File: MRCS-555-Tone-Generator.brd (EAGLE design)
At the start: 50 x 50 mm, 19 parts, among them CON1 5V input, CON2 5 V input, CON3 output 3.5mm, CON4 Output 0.100, IC1 NE555

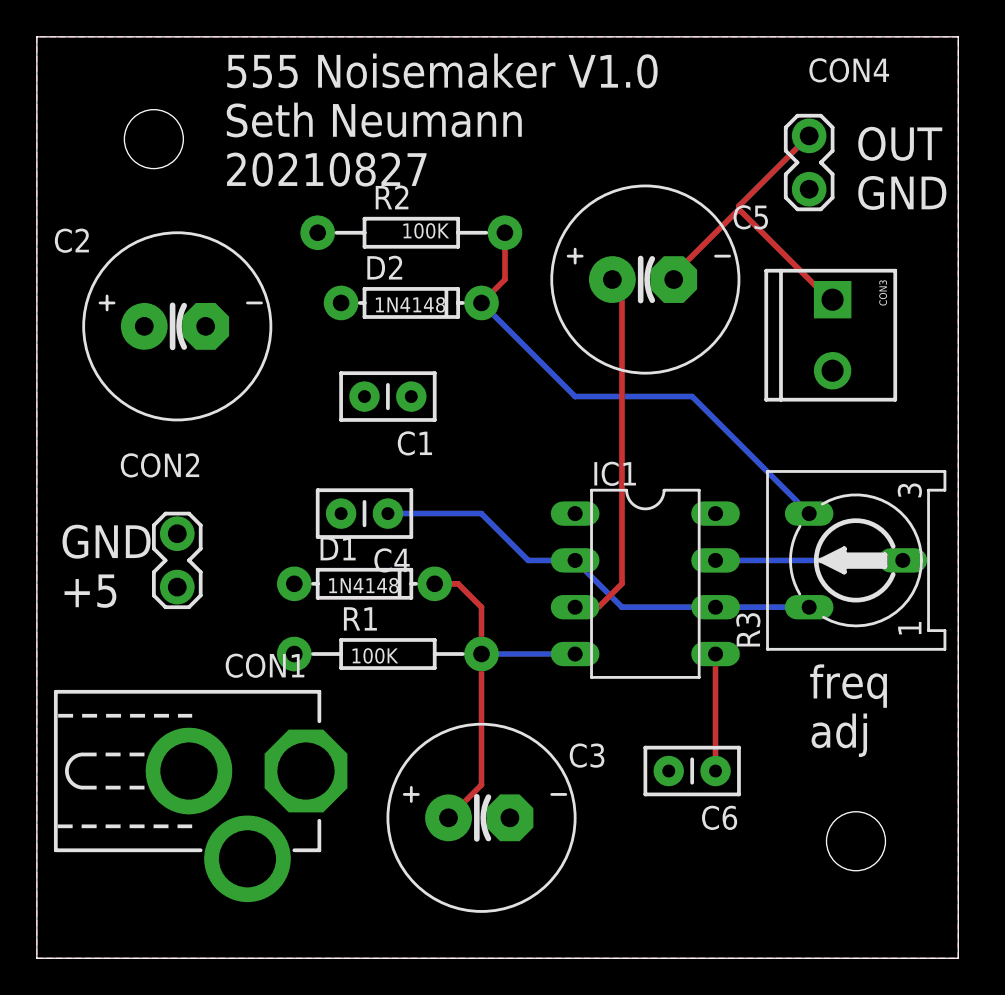
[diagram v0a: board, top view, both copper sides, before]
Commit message: Updates after first article tested good
clean up of some nomenclature
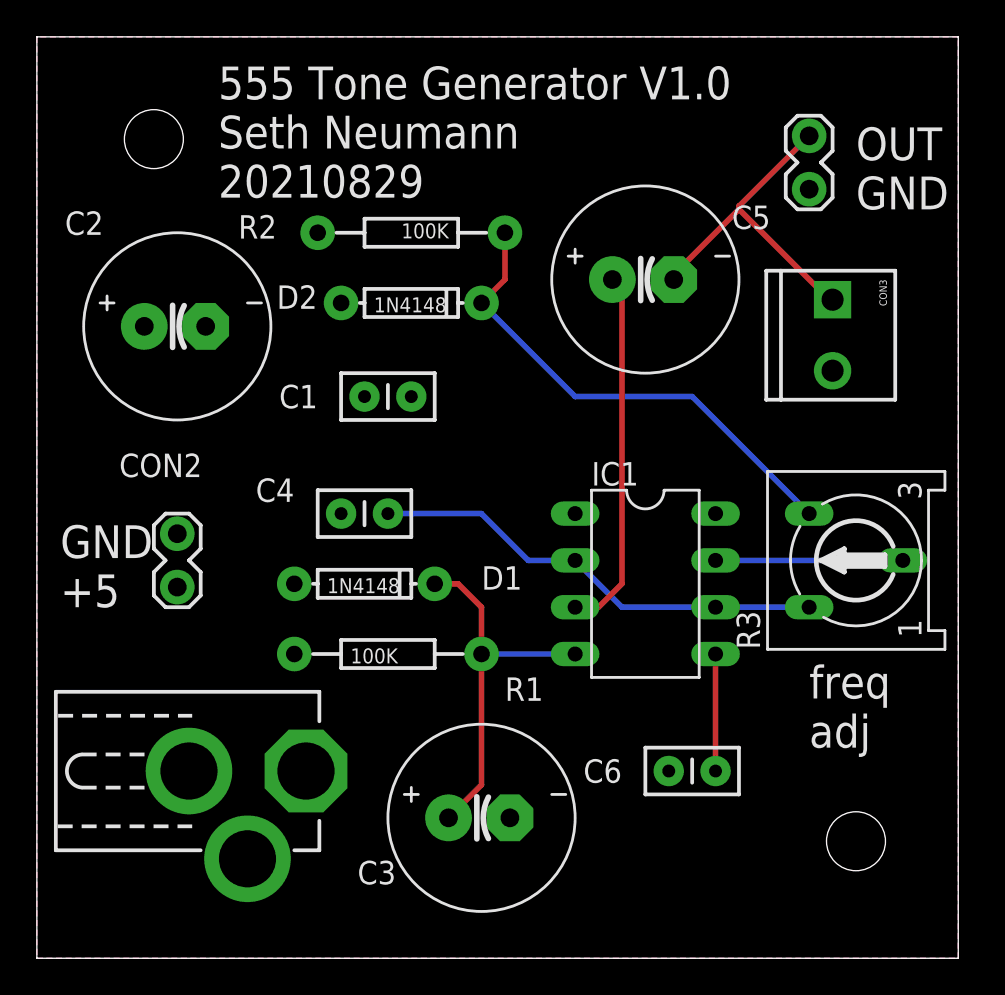
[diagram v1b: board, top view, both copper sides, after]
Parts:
- C1: value 0.01 uF 103 -> .01uF
- C4: value 0.01 103 -> 0.01uF
- C6: value 0.01 uF 103 -> 0.01uF
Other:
- board text added: "555 Tone Generator V1.0 Seth Neumann 20210829"
- board text removed: "555 Noisemaker V1.0 Seth Neumann 20210827"
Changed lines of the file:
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@@
 <setting verticaltext="up"/>
 </settings>
-<grid distance="25" unitdist="mil" unit="mil" style="dots" multiple="2" display="yes" altdistance="12.5" altunitdist="mil" altunit="mil"/>
+<grid distance="50" unitdist="mil" unit="mil" style="dots" multiple="2" display="yes" altdistance="12.5" altunitdist="mil" altunit="mil"/>
 <layers>
 <layer number="1" name="Top" color="4" fill="1" visible="yes" active="yes"/>
@@
 <hole x="6.35" y="44.45" drill="3.2"/>
 <hole x="44.45" y="6.35" drill="3.2"/>
-<text x="10.16" y="41.91" size="1.778" layer="21" font="vector" ratio="10">555 Noisemaker V1.0
+<text x="9.8425" y="41.275" size="1.778" layer="21" font="vector" ratio="10">555 Tone Generator V1.0
 Seth Neumann
-20210827</text>
+20210829</text>
 <text x="41.91" y="11.43" size="1.778" layer="21" font="vector" ratio="10">freq
 adj</text>
@@
 <element name="CON2" library="SPCoast" package="1X02_LOCK" value="5 V input" x="7.62" y="20.32" smashed="yes" rot="R90">
 <attribute name="NAME" x="8.9662" y="27.3812" size="1.27" layer="25" ratio="10" rot="R180"/>
-<attribute name="VALUE" x="12.065" y="19.05" size="1.27" layer="27" rot="R90"/>
 </element>
 <element name="CON3" library="SPCoast" package="SCREWTERMINAL-3.5MM-2_LOCK" value="output 3.5mm" x="43.18" y="35.56" rot="R270"/>
 <element name="D1" library="SPCoast" package="DIODE-1N4148" value="1N4148" x="17.78" y="20.32" smashed="yes" rot="R180">
-<attribute name="NAME" x="15.24" y="21.59" size="1.27" layer="25"/>
+<attribute name="NAME" x="24.13" y="20.0025" size="1.27" layer="25"/>
 <attribute name="VALUE" x="15.748" y="19.812" size="0.8128" layer="21"/>
 </element>
 <element name="D2" library="SPCoast" package="DIODE-1N4148" value="1N4148" x="20.32" y="35.56" smashed="yes" rot="R180">
-<attribute name="NAME" x="17.78" y="36.83" size="1.27" layer="25"/>
+<attribute name="NAME" x="13.0175" y="35.2425" size="1.27" layer="25"/>
 <attribute name="VALUE" x="18.288" y="35.052" size="0.8128" layer="21"/>
 </element>
@@
 </element>
 <element name="R2" library="SPCoast" package="AXIAL-0.4-RES" value="100K" x="20.32" y="39.37" smashed="yes" rot="R180">
-<attribute name="NAME" x="20.32" y="41.91" size="1.27" layer="25" rot="R180"/>
+<attribute name="NAME" x="13.0175" y="40.3225" size="1.27" layer="25" rot="R180"/>
 <attribute name="VALUE" x="22.352" y="39.878" size="0.8128" layer="21" ratio="15" rot="R180"/>
 </element>
 <element name="R1" library="SPCoast" package="AXIAL-0.4-RES" value="100K" x="19.05" y="16.51" smashed="yes">
-<attribute name="NAME" x="16.51" y="17.78" size="1.27" layer="25"/>
+<attribute name="NAME" x="25.4" y="13.97" size="1.27" layer="25"/>
 <attribute name="VALUE" x="17.018" y="16.002" size="0.8128" layer="21" ratio="15"/>
 </element>
 <element name="C2" library="SPCoast" package="E3.5-10" value="100 uF" x="7.62" y="34.29" smashed="yes">
-<attribute name="NAME" x="0.889" y="38.3032" size="1.27" layer="25" ratio="10"/>
+<attribute name="NAME" x="1.524" y="39.2557" size="1.27" layer="25" ratio="10"/>
 <attribute name="VALUE" x="4.4958" y="31.0642" size="1.27" layer="27" ratio="10"/>
 </element>
-<element name="C4" library="SPCoast" package="C-PTH-0.100" value="0.01 103" x="17.78" y="24.13" smashed="yes" rot="R180">
-<attribute name="NAME" x="20.32" y="22.225" size="1.27" layer="25" rot="R180"/>
-<attribute name="VALUE" x="20.32" y="26.67" size="0.6096" layer="27" rot="R180"/>
+<element name="C4" library="SPCoast" package="C-PTH-0.100" value="0.01uF" x="17.78" y="24.13" smashed="yes" rot="R180">
+<attribute name="NAME" x="13.97" y="26.035" size="1.27" layer="25" rot="R180"/>
+<attribute name="VALUE" x="26.67" y="25.4" size="1.27" layer="27" rot="R180"/>
 </element>
 <element name="R3" library="MRCS" package="RS3" value="100K" x="44.45" y="21.59" rot="R90"/>
-<element name="CON1" library="SPCoast" package="DCJ0202" value="5V input" x="11.43" y="10.16" rot="R270"/>
-<element name="CON4" library="SPCoast" package="1X02_LOCK" value="Output 0.100" x="41.91" y="44.45" smashed="yes" rot="R270">
-<attribute name="NAME" x="41.8338" y="47.5488" size="1.27" layer="25" ratio="10"/>
-</element>
-<element name="C1" library="SPCoast" package="C-PTH-0.100" value="0.01 uF 103" x="19.05" y="30.48" smashed="yes" rot="R180">
-<attribute name="NAME" x="21.59" y="28.575" size="1.27" layer="25" rot="R180"/>
-<attribute name="VALUE" x="21.59" y="33.02" size="0.6096" layer="27" rot="R180"/>
-</element>
-<element name="C6" library="SPCoast" package="C-PTH-0.100" value="0.01 uF 103" x="35.56" y="10.16" smashed="yes" rot="R180">
-<attribute name="NAME" x="38.1" y="8.255" size="1.27" layer="25" rot="R180"/>
-<attribute name="VALUE" x="38.1" y="12.7" size="0.6096" layer="27" rot="R180"/>
+<element name="CON1" library="SPCoast" package="DCJ0202" value="5V input" x="11.43" y="10.16" smashed="yes" rot="R270">
+<attribute name="VALUE" x="1.27" y="15.24" size="1.27" layer="27"/>
+</element>
+<element name="CON4" library="SPCoast" package="1X02_LOCK" value="Output 0.100" x="41.91" y="44.45" smashed="yes" rot="R270"/>
+<element name="C1" library="SPCoast" package="C-PTH-0.100" value=".01uF" x="19.05" y="30.48" smashed="yes" rot="R180">
+<attribute name="NAME" x="15.24" y="31.115" size="1.27" layer="25" rot="R180"/>
+<attribute name="VALUE" x="26.67" y="31.75" size="1.27" layer="27" rot="R180"/>
+</element>
+<element name="C6" library="SPCoast" package="C-PTH-0.100" value="0.01uF " x="35.56" y="10.16" smashed="yes" rot="R180">
+<attribute name="NAME" x="31.75" y="10.795" size="1.27" layer="25" rot="R180"/>
+<attribute name="VALUE" x="39.37" y="13.97" size="1.27" layer="27" rot="R180"/>
 </element>
 <element name="C5" library="SPCoast" package="E3.5-10" value="100 uF" x="33.02" y="36.83"/>
-<element name="C3" library="SPCoast" package="E3.5-10" value="10 uF" x="24.13" y="7.62"/>
+<element name="C3" library="SPCoast" package="E3.5-10" value="10 uF" x="24.13" y="7.62" smashed="yes">
+<attribute name="NAME" x="17.399" y="4.0132" size="1.27" layer="25" ratio="10"/>
+<attribute name="VALUE" x="21.0058" y="4.3942" size="1.27" layer="27" ratio="10"/>
+</element>
 <element name="U$1" library="MRCSLogoTop" package="MRCSLOGOTOP" value="" x="31.75" y="1.27"/>
 <element name="U$2" library="MRCSLogoBtm" package="MRCSLOGOBTM" value="" x="31.75" y="1.27"/>

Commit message: Minor updates after building 1st articles
Changed C3 from electrolytic to 0.1 for Tant or Monolithic
Minor clean up of labels on board
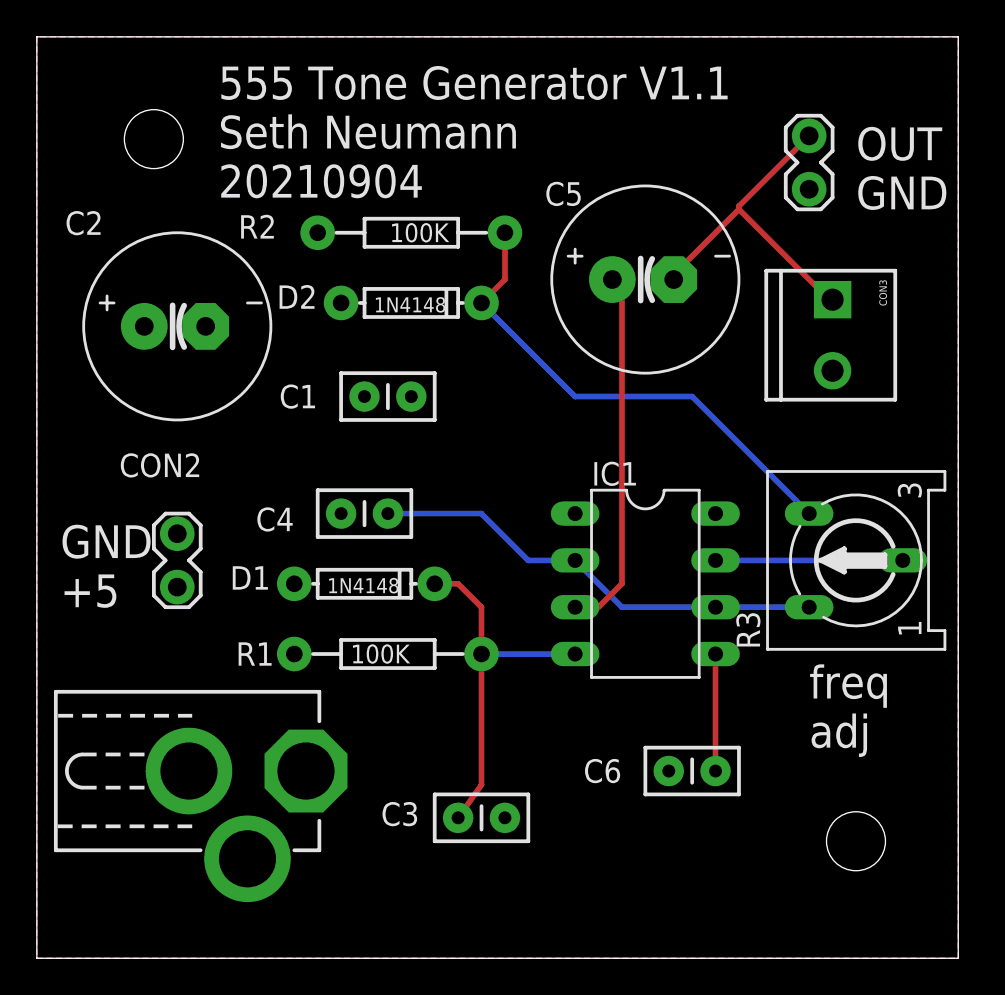
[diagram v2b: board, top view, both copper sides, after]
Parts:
- C1: value .01uF -> 0.01uF
- C3: device SPCoast:E3.5-10 -> SPCoast:C-PTH-0.100
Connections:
- net GND: now also C3.2; no longer C3.-
- net N$6: now also C3.1; no longer C3.+
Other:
- board text added: "555 Tone Generator V1.1 Seth Neumann 20210904"
- board text removed: "555 Tone Generator V1.0 Seth Neumann 20210829"
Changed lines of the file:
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@@
 <hole x="6.35" y="44.45" drill="3.2"/>
 <hole x="44.45" y="6.35" drill="3.2"/>
-<text x="9.8425" y="41.275" size="1.778" layer="21" font="vector" ratio="10">555 Tone Generator V1.0
+<text x="9.8425" y="41.275" size="1.778" layer="21" font="vector" ratio="10">555 Tone Generator V1.1
 Seth Neumann
-20210829</text>
+20210904</text>
 <text x="41.91" y="11.43" size="1.778" layer="21" font="vector" ratio="10">freq
 adj</text>
@@
 <element name="CON3" library="SPCoast" package="SCREWTERMINAL-3.5MM-2_LOCK" value="output 3.5mm" x="43.18" y="35.56" rot="R270"/>
 <element name="D1" library="SPCoast" package="DIODE-1N4148" value="1N4148" x="17.78" y="20.32" smashed="yes" rot="R180">
-<attribute name="NAME" x="24.13" y="20.0025" size="1.27" layer="25"/>
+<attribute name="NAME" x="10.4775" y="20.0025" size="1.27" layer="25"/>
 <attribute name="VALUE" x="15.748" y="19.812" size="0.8128" layer="21"/>
 </element>
@@
 <element name="R2" library="SPCoast" package="AXIAL-0.4-RES" value="100K" x="20.32" y="39.37" smashed="yes" rot="R180">
 <attribute name="NAME" x="13.0175" y="40.3225" size="1.27" layer="25" rot="R180"/>
-<attribute name="VALUE" x="22.352" y="39.878" size="0.8128" layer="21" ratio="15" rot="R180"/>
+<attribute name="VALUE" x="22.352" y="39.878" size="1.016" layer="21" ratio="15" rot="R180"/>
 </element>
 <element name="R1" library="SPCoast" package="AXIAL-0.4-RES" value="100K" x="19.05" y="16.51" smashed="yes">
-<attribute name="NAME" x="25.4" y="13.97" size="1.27" layer="25"/>
-<attribute name="VALUE" x="17.018" y="16.002" size="0.8128" layer="21" ratio="15"/>
+<attribute name="NAME" x="10.795" y="15.875" size="1.27" layer="25"/>
+<attribute name="VALUE" x="17.018" y="16.002" size="1.016" layer="21" ratio="15"/>
 </element>
 <element name="C2" library="SPCoast" package="E3.5-10" value="100 uF" x="7.62" y="34.29" smashed="yes">
@@
 </element>
 <element name="C4" library="SPCoast" package="C-PTH-0.100" value="0.01uF" x="17.78" y="24.13" smashed="yes" rot="R180">
-<attribute name="NAME" x="13.97" y="26.035" size="1.27" layer="25" rot="R180"/>
+<attribute name="NAME" x="13.97" y="24.4475" size="1.27" layer="25" rot="R180"/>
 <attribute name="VALUE" x="26.67" y="25.4" size="1.27" layer="27" rot="R180"/>
 </element>
@@
 </element>
 <element name="CON4" library="SPCoast" package="1X02_LOCK" value="Output 0.100" x="41.91" y="44.45" smashed="yes" rot="R270"/>
-<element name="C1" library="SPCoast" package="C-PTH-0.100" value=".01uF" x="19.05" y="30.48" smashed="yes" rot="R180">
+<element name="C1" library="SPCoast" package="C-PTH-0.100" value="0.01uF" x="19.05" y="30.48" smashed="yes" rot="R180">
 <attribute name="NAME" x="15.24" y="31.115" size="1.27" layer="25" rot="R180"/>
-<attribute name="VALUE" x="26.67" y="31.75" size="1.27" layer="27" rot="R180"/>
+<attribute name="VALUE" x="27.94" y="31.75" size="1.27" layer="27" rot="R180"/>
 </element>
 <element name="C6" library="SPCoast" package="C-PTH-0.100" value="0.01uF " x="35.56" y="10.16" smashed="yes" rot="R180">
@@
 <attribute name="VALUE" x="39.37" y="13.97" size="1.27" layer="27" rot="R180"/>
 </element>
-<element name="C5" library="SPCoast" package="E3.5-10" value="100 uF" x="33.02" y="36.83"/>
-<element name="C3" library="SPCoast" package="E3.5-10" value="10 uF" x="24.13" y="7.62" smashed="yes">
-<attribute name="NAME" x="17.399" y="4.0132" size="1.27" layer="25" ratio="10"/>
+<element name="C5" library="SPCoast" package="E3.5-10" value="100 uF" x="33.02" y="36.83" smashed="yes">
+<attribute name="NAME" x="27.559" y="40.8432" size="1.27" layer="25" ratio="10"/>
+<attribute name="VALUE" x="29.8958" y="33.6042" size="1.27" layer="27" ratio="10"/>
+</element>
+<element name="C3" library="SPCoast" package="C-PTH-0.100" value="10 uF" x="24.13" y="7.62" smashed="yes">
+<attribute name="NAME" x="18.669" y="7.1882" size="1.27" layer="25" ratio="10"/>
 <attribute name="VALUE" x="21.0058" y="4.3942" size="1.27" layer="27" ratio="10"/>
 </element>
@@
 <contactref element="C6" pad="2"/>
 <contactref element="R1" pad="P$1"/>
-<contactref element="C3" pad="-"/>
+<contactref element="C3" pad="2"/>
 <contactref element="C4" pad="2"/>
 <polygon width="0.4064" layer="16" isolate="0.6096">
@@
 <contactref element="R1" pad="P$2"/>
 <contactref element="IC1" pad="4"/>
-<contactref element="C3" pad="+"/>
+<contactref element="C3" pad="1"/>
 <wire x1="21.59" y1="20.32" x2="22.86" y2="20.32" width="0.3048" layer="1"/>
 <wire x1="22.86" y1="20.32" x2="24.13" y2="19.05" width="0.3048" layer="1"/>
 <wire x1="24.13" y1="19.05" x2="24.13" y2="16.51" width="0.3048" layer="1"/>
 <wire x1="24.13" y1="16.51" x2="24.13" y2="9.41" width="0.3048" layer="1"/>
-<wire x1="24.13" y1="9.41" x2="22.34" y2="7.62" width="0.3048" layer="1"/>
+<wire x1="24.13" y1="9.41" x2="22.86" y2="7.62" width="0.3048" layer="1"/>
 <wire x1="24.13" y1="16.51" x2="29.21" y2="16.51" width="0.3048" layer="16"/>
 </signal>
